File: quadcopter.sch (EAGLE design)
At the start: 65 parts, among them J1 AVR_SPI_PRG_6NS, U1 ATMEGA128RFA1, Y2 16MHz

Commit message: pinned up IMU
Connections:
- removed net VDD: C23.1, C24.1, U$8.VDD1, U$8.VDD2
- removed net VDDIO: C21.1, R12.2, R13.2, U$8.VDDIO1, U$8.VDDIO2
- net 3V: now also C21.1, C23.1, C24.1, R12.2, R13.2, U$8.CS_A/G, U$8.CS_M, U$8.DEN_A/G, U$8.DRDY_M, U$8.VDD1, U$8.VDD2, U$8.VDDIO1, U$8.VDDIO2
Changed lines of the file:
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@@
 <label x="193.04" y="30.48" size="1.778" layer="95" rot="R180" xref="yes"/>
+</segment>
+<segment>
+<pinref part="C21" gate="G$1" pin="1"/>
+<wire x1="180.34" y1="55.88" x2="180.34" y2="60.96" width="0.1524" layer="91"/>
+<label x="180.34" y="66.04" size="1.778" layer="95" rot="R90" xref="yes"/>
+<pinref part="U$8" gate="G$1" pin="VDDIO1"/>
+<wire x1="180.34" y1="60.96" x2="180.34" y2="66.04" width="0.1524" layer="91"/>
+<wire x1="220.98" y1="45.72" x2="220.98" y2="50.8" width="0.1524" layer="91"/>
+<pinref part="R12" gate="G$1" pin="2"/>
+<wire x1="220.98" y1="50.8" x2="220.98" y2="53.34" width="0.1524" layer="91"/>
+<wire x1="203.2" y1="50.8" x2="220.98" y2="50.8" width="0.1524" layer="91"/>
+<pinref part="R13" gate="G$1" pin="2"/>
+<wire x1="187.96" y1="50.8" x2="187.96" y2="53.34" width="0.1524" layer="91"/>
+<wire x1="187.96" y1="53.34" x2="220.98" y2="53.34" width="0.1524" layer="91"/>
+<wire x1="180.34" y1="60.96" x2="220.98" y2="60.96" width="0.1524" layer="91"/>
+<wire x1="220.98" y1="60.96" x2="220.98" y2="53.34" width="0.1524" layer="91"/>
+<junction x="180.34" y="60.96"/>
+<junction x="220.98" y="53.34"/>
+<junction x="220.98" y="50.8"/>
+</segment>
+<segment>
+<pinref part="U$8" gate="G$1" pin="VDDIO2"/>
+<wire x1="213.36" y1="35.56" x2="200.66" y2="35.56" width="0.1524" layer="91"/>
+<label x="200.66" y="35.56" size="1.778" layer="95" rot="R180" xref="yes"/>
+</segment>
+<segment>
+<pinref part="U$8" gate="G$1" pin="VDD1"/>
+<wire x1="226.06" y1="45.72" x2="226.06" y2="60.96" width="0.1524" layer="91"/>
+<pinref part="U$8" gate="G$1" pin="VDD2"/>
+<wire x1="228.6" y1="45.72" x2="228.6" y2="60.96" width="0.1524" layer="91"/>
+<wire x1="226.06" y1="60.96" x2="228.6" y2="60.96" width="0.1524" layer="91"/>
+<wire x1="228.6" y1="60.96" x2="228.6" y2="101.6" width="0.1524" layer="91"/>
+<pinref part="C24" gate="G$1" pin="1"/>
+<pinref part="C23" gate="G$1" pin="1"/>
+<wire x1="213.36" y1="96.52" x2="213.36" y2="99.06" width="0.1524" layer="91"/>
+<wire x1="213.36" y1="99.06" x2="205.74" y2="99.06" width="0.1524" layer="91"/>
+<wire x1="205.74" y1="99.06" x2="205.74" y2="96.52" width="0.1524" layer="91"/>
+<wire x1="228.6" y1="101.6" x2="213.36" y2="101.6" width="0.1524" layer="91"/>
+<wire x1="213.36" y1="101.6" x2="213.36" y2="99.06" width="0.1524" layer="91"/>
+<wire x1="213.36" y1="101.6" x2="213.36" y2="106.68" width="0.1524" layer="91"/>
+<junction x="213.36" y="99.06"/>
+<junction x="213.36" y="101.6"/>
+<junction x="228.6" y="60.96"/>
+<label x="213.36" y="106.68" size="1.778" layer="95" rot="R90" xref="yes"/>
+</segment>
+<segment>
+<pinref part="U$8" gate="G$1" pin="CS_A/G"/>
+<wire x1="223.52" y1="22.86" x2="223.52" y2="12.7" width="0.1524" layer="91"/>
+<wire x1="223.52" y1="12.7" x2="226.06" y2="12.7" width="0.1524" layer="91"/>
+<wire x1="226.06" y1="12.7" x2="228.6" y2="12.7" width="0.1524" layer="91"/>
+<wire x1="228.6" y1="12.7" x2="238.76" y2="12.7" width="0.1524" layer="91"/>
+<wire x1="238.76" y1="12.7" x2="241.3" y2="12.7" width="0.1524" layer="91"/>
+<wire x1="241.3" y1="12.7" x2="241.3" y2="10.16" width="0.1524" layer="91"/>
+<pinref part="U$8" gate="G$1" pin="CS_M"/>
+<wire x1="226.06" y1="22.86" x2="226.06" y2="12.7" width="0.1524" layer="91"/>
+<pinref part="U$8" gate="G$1" pin="DRDY_M"/>
+<wire x1="228.6" y1="22.86" x2="228.6" y2="12.7" width="0.1524" layer="91"/>
+<pinref part="U$8" gate="G$1" pin="DEN_A/G"/>
+<wire x1="238.76" y1="22.86" x2="238.76" y2="12.7" width="0.1524" layer="91"/>
+<junction x="226.06" y="12.7"/>
+<junction x="228.6" y="12.7"/>
+<junction x="238.76" y="12.7"/>
+<label x="241.3" y="10.16" size="1.778" layer="95" rot="R270" xref="yes"/>
 </segment>
 </net>
@@
 <wire x1="200.66" y1="38.1" x2="200.66" y2="40.64" width="0.1524" layer="91"/>
 <wire x1="200.66" y1="40.64" x2="198.12" y2="40.64" width="0.1524" layer="91"/>
+<junction x="203.2" y="38.1"/>
 </segment>
 </net>
@@
 <wire x1="187.96" y1="33.02" x2="185.42" y2="33.02" width="0.1524" layer="91"/>
 <label x="185.42" y="33.02" size="1.778" layer="95" rot="R180" xref="yes"/>
+<junction x="187.96" y="33.02"/>
 </segment>
 </net>
@@
 </segment>
 </net>
-<net name="VDDIO" class="0">
-<segment>
-<pinref part="U$8" gate="G$1" pin="VDDIO2"/>
-<wire x1="213.36" y1="35.56" x2="200.66" y2="35.56" width="0.1524" layer="91"/>
-<label x="200.66" y="35.56" size="1.778" layer="95" rot="R180" xref="yes"/>
-</segment>
-<segment>
-<pinref part="C21" gate="G$1" pin="1"/>
-<wire x1="180.34" y1="55.88" x2="180.34" y2="60.96" width="0.1524" layer="91"/>
-<label x="180.34" y="66.04" size="1.778" layer="95" rot="R90" xref="yes"/>
-<pinref part="U$8" gate="G$1" pin="VDDIO1"/>
-<wire x1="180.34" y1="60.96" x2="180.34" y2="66.04" width="0.1524" layer="91"/>
-<wire x1="220.98" y1="45.72" x2="220.98" y2="50.8" width="0.1524" layer="91"/>
-<pinref part="R12" gate="G$1" pin="2"/>
-<wire x1="220.98" y1="50.8" x2="220.98" y2="53.34" width="0.1524" layer="91"/>
-<wire x1="203.2" y1="50.8" x2="220.98" y2="50.8" width="0.1524" layer="91"/>
-<pinref part="R13" gate="G$1" pin="2"/>
-<wire x1="187.96" y1="50.8" x2="187.96" y2="53.34" width="0.1524" layer="91"/>
-<wire x1="187.96" y1="53.34" x2="220.98" y2="53.34" width="0.1524" layer="91"/>
-<wire x1="180.34" y1="60.96" x2="220.98" y2="60.96" width="0.1524" layer="91"/>
-<wire x1="220.98" y1="60.96" x2="220.98" y2="53.34" width="0.1524" layer="91"/>
-<junction x="180.34" y="60.96"/>
-<junction x="220.98" y="53.34"/>
-<junction x="220.98" y="50.8"/>
-</segment>
-</net>
 <net name="N$20" class="0">
 <segment>
@@
 </segment>
 </net>
-<net name="VDD" class="0">
-<segment>
-<pinref part="U$8" gate="G$1" pin="VDD1"/>
-<wire x1="226.06" y1="45.72" x2="226.06" y2="60.96" width="0.1524" layer="91"/>
-<pinref part="U$8" gate="G$1" pin="VDD2"/>
-<wire x1="228.6" y1="45.72" x2="228.6" y2="60.96" width="0.1524" layer="91"/>
-<wire x1="226.06" y1="60.96" x2="228.6" y2="60.96" width="0.1524" layer="91"/>
-<wire x1="228.6" y1="60.96" x2="228.6" y2="101.6" width="0.1524" layer="91"/>
-<pinref part="C24" gate="G$1" pin="1"/>
-<pinref part="C23" gate="G$1" pin="1"/>
-<wire x1="213.36" y1="96.52" x2="213.36" y2="99.06" width="0.1524" layer="91"/>
-<wire x1="213.36" y1="99.06" x2="205.74" y2="99.06" width="0.1524" layer="91"/>
-<wire x1="205.74" y1="99.06" x2="205.74" y2="96.52" width="0.1524" layer="91"/>
-<wire x1="228.6" y1="101.6" x2="213.36" y2="101.6" width="0.1524" layer="91"/>
-<wire x1="213.36" y1="101.6" x2="213.36" y2="99.06" width="0.1524" layer="91"/>
-<wire x1="213.36" y1="101.6" x2="213.36" y2="106.68" width="0.1524" layer="91"/>
-<junction x="213.36" y="99.06"/>
-<junction x="213.36" y="101.6"/>
-<junction x="228.6" y="60.96"/>
-<label x="213.36" y="106.68" size="1.778" layer="95" rot="R90" xref="yes"/>
-</segment>
-</net>

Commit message: pushing who am i and final changes to the IMU
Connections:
- net 3V: no longer U$8.DRDY_M
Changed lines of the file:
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@@
 <wire x1="223.52" y1="22.86" x2="223.52" y2="12.7" width="0.1524" layer="91"/>
 <wire x1="223.52" y1="12.7" x2="226.06" y2="12.7" width="0.1524" layer="91"/>
-<wire x1="226.06" y1="12.7" x2="228.6" y2="12.7" width="0.1524" layer="91"/>
-<wire x1="228.6" y1="12.7" x2="238.76" y2="12.7" width="0.1524" layer="91"/>
+<wire x1="226.06" y1="12.7" x2="238.76" y2="12.7" width="0.1524" layer="91"/>
 <wire x1="238.76" y1="12.7" x2="241.3" y2="12.7" width="0.1524" layer="91"/>
 <wire x1="241.3" y1="12.7" x2="241.3" y2="10.16" width="0.1524" layer="91"/>
 <pinref part="U$8" gate="G$1" pin="CS_M"/>
 <wire x1="226.06" y1="22.86" x2="226.06" y2="12.7" width="0.1524" layer="91"/>
-<pinref part="U$8" gate="G$1" pin="DRDY_M"/>
-<wire x1="228.6" y1="22.86" x2="228.6" y2="12.7" width="0.1524" layer="91"/>
 <pinref part="U$8" gate="G$1" pin="DEN_A/G"/>
 <wire x1="238.76" y1="22.86" x2="238.76" y2="12.7" width="0.1524" layer="91"/>
 <junction x="226.06" y="12.7"/>
-<junction x="228.6" y="12.7"/>
 <junction x="238.76" y="12.7"/>
 <label x="241.3" y="10.16" size="1.778" layer="95" rot="R270" xref="yes"/>

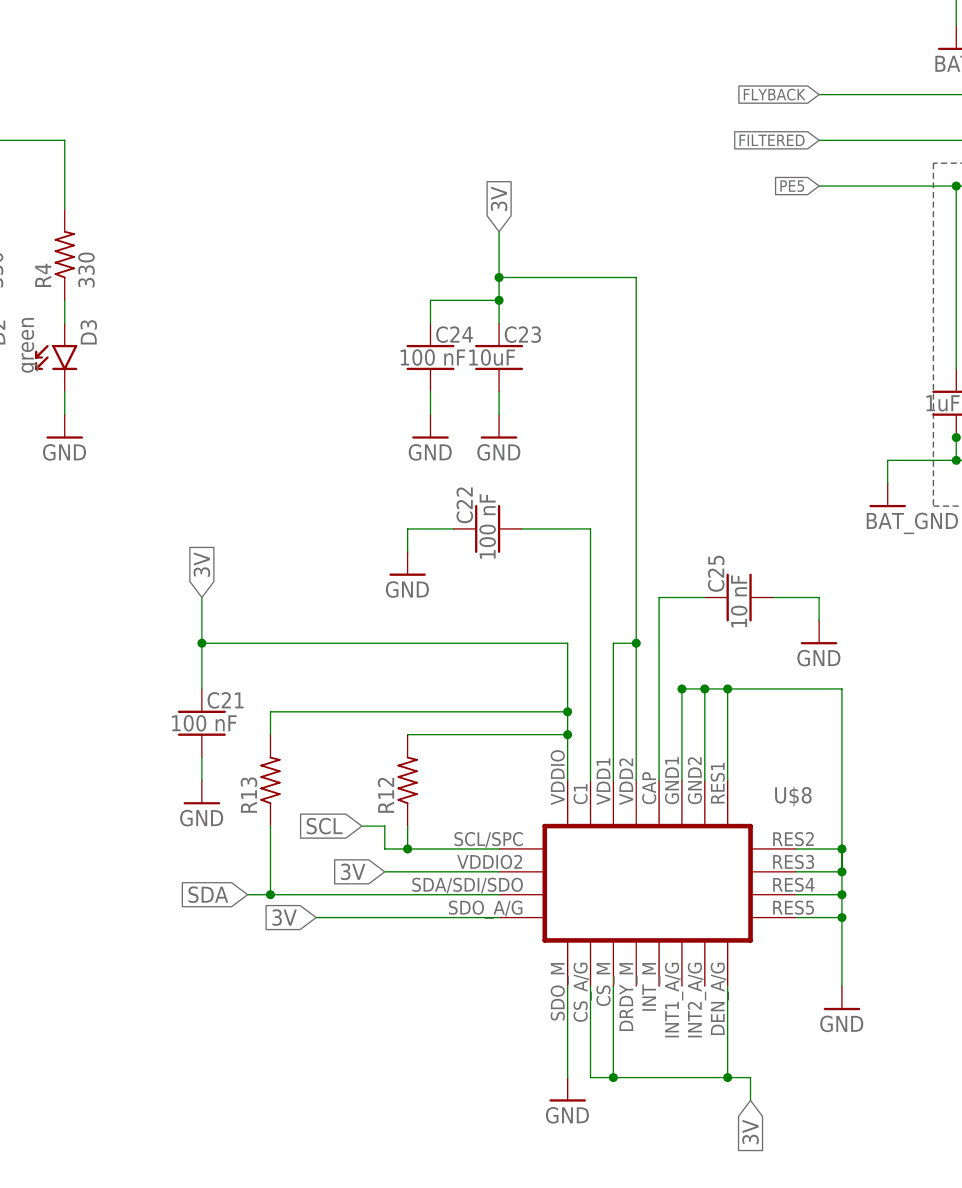
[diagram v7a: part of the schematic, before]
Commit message: Small fixes for IMU, added PID to who_am_i
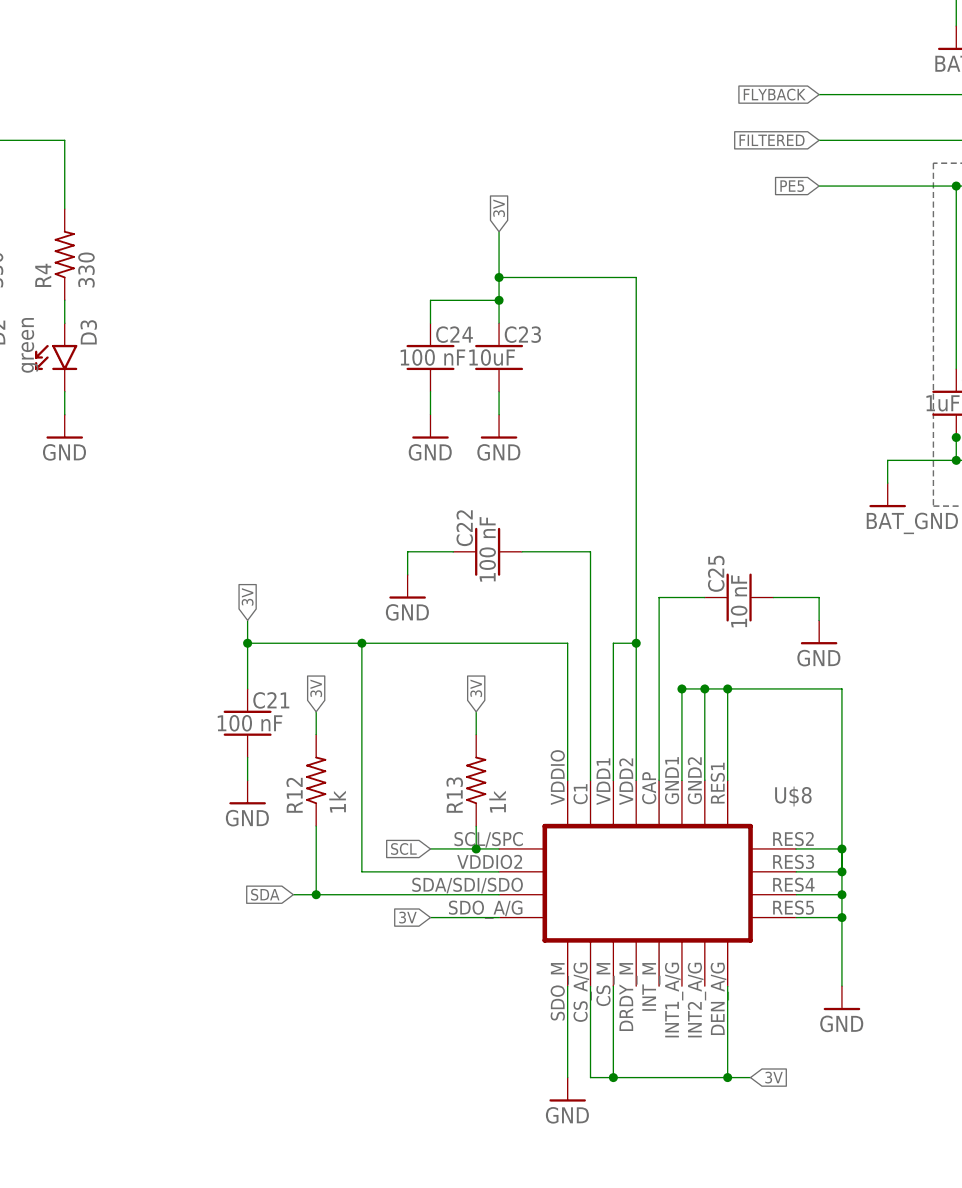
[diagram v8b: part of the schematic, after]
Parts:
- R12, R13: value (none) -> 1k
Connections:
- net SCL: now also R13.1; no longer R12.1
- net SDA: now also R12.1; no longer R13.1
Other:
- moved on the sheet: C21, C22, R12, R13
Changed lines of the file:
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@@
 <part name="U$7" library="quadparts" deviceset="MOSFET_20V" device=""/>
 <part name="U$8" library="quadparts" deviceset="IMU_9AXIS" device=""/>
-<part name="R12" library="quadparts_prebuilt" deviceset="RESISTOR_" device="SMD-2012-0805"/>
-<part name="R13" library="quadparts_prebuilt" deviceset="RESISTOR_" device="SMD-2012-0805"/>
 <part name="GND33" library="quadparts_prebuilt" deviceset="GND" device=""/>
 <part name="C21" library="quadparts_prebuilt" deviceset="CAPACITOR-NP_" device="SMD-2012-0805_CERAMIC" value="100 nF"/>
@@
 <part name="GND38" library="quadparts_prebuilt" deviceset="GND" device=""/>
 <part name="GND39" library="quadparts_prebuilt" deviceset="GND" device=""/>
+<part name="R12" library="quadparts_prebuilt" deviceset="RESISTOR_" device="SMD-2012-0805" value="1k"/>
+<part name="R13" library="quadparts_prebuilt" deviceset="RESISTOR_" device="SMD-2012-0805" value="1k"/>
 </parts>
 <sheets>
@@
 <instance part="U$7" gate="G$1" x="396.24" y="101.6"/>
 <instance part="U$8" gate="G$1" x="220.98" y="45.72"/>
-<instance part="R12" gate="G$1" x="203.2" y="45.72" rot="R90"/>
-<instance part="R13" gate="G$1" x="187.96" y="45.72" rot="R90"/>
 <instance part="GND33" gate="1" x="251.46" y="20.32"/>
-<instance part="C21" gate="G$1" x="180.34" y="53.34"/>
-<instance part="GND34" gate="1" x="180.34" y="43.18"/>
-<instance part="C22" gate="G$1" x="210.82" y="73.66" rot="R90"/>
-<instance part="GND35" gate="1" x="203.2" y="68.58"/>
+<instance part="C21" gate="G$1" x="185.42" y="53.34"/>
+<instance part="GND34" gate="1" x="185.42" y="43.18"/>
+<instance part="C22" gate="G$1" x="210.82" y="71.12" rot="R90"/>
+<instance part="GND35" gate="1" x="203.2" y="66.04"/>
 <instance part="GND36" gate="1" x="205.74" y="83.82"/>
 <instance part="GND37" gate="1" x="213.36" y="83.82"/>
@@
 <instance part="GND38" gate="1" x="248.92" y="60.96"/>
 <instance part="GND39" gate="1" x="220.98" y="10.16"/>
+<instance part="R12" gate="G$1" x="193.04" y="45.72" rot="R90"/>
+<instance part="R13" gate="G$1" x="210.82" y="45.72" rot="R90"/>
 </instances>
 <busses>
@@
 <segment>
 <pinref part="U$8" gate="G$1" pin="SDO_A/G"/>
-<wire x1="193.04" y1="30.48" x2="213.36" y2="30.48" width="0.1524" layer="91"/>
-<label x="193.04" y="30.48" size="1.778" layer="95" rot="R180" xref="yes"/>
+<wire x1="205.74" y1="30.48" x2="213.36" y2="30.48" width="0.1524" layer="91"/>
+<label x="205.74" y="30.48" size="1.27" layer="95" rot="R180" xref="yes"/>
 </segment>
 <segment>
 <pinref part="C21" gate="G$1" pin="1"/>
-<wire x1="180.34" y1="55.88" x2="180.34" y2="60.96" width="0.1524" layer="91"/>
-<label x="180.34" y="66.04" size="1.778" layer="95" rot="R90" xref="yes"/>
+<wire x1="185.42" y1="55.88" x2="185.42" y2="60.96" width="0.1524" layer="91"/>
+<label x="185.42" y="63.5" size="1.27" layer="95" rot="R90" xref="yes"/>
 <pinref part="U$8" gate="G$1" pin="VDDIO1"/>
-<wire x1="180.34" y1="60.96" x2="180.34" y2="66.04" width="0.1524" layer="91"/>
-<wire x1="220.98" y1="45.72" x2="220.98" y2="50.8" width="0.1524" layer="91"/>
-<pinref part="R12" gate="G$1" pin="2"/>
-<wire x1="220.98" y1="50.8" x2="220.98" y2="53.34" width="0.1524" layer="91"/>
-<wire x1="203.2" y1="50.8" x2="220.98" y2="50.8" width="0.1524" layer="91"/>
-<pinref part="R13" gate="G$1" pin="2"/>
-<wire x1="187.96" y1="50.8" x2="187.96" y2="53.34" width="0.1524" layer="91"/>
-<wire x1="187.96" y1="53.34" x2="220.98" y2="53.34" width="0.1524" layer="91"/>
-<wire x1="180.34" y1="60.96" x2="220.98" y2="60.96" width="0.1524" layer="91"/>
-<wire x1="220.98" y1="60.96" x2="220.98" y2="53.34" width="0.1524" layer="91"/>
-<junction x="180.34" y="60.96"/>
-<junction x="220.98" y="53.34"/>
-<junction x="220.98" y="50.8"/>
-</segment>
-<segment>
+<wire x1="185.42" y1="60.96" x2="185.42" y2="63.5" width="0.1524" layer="91"/>
+<wire x1="185.42" y1="60.96" x2="198.12" y2="60.96" width="0.1524" layer="91"/>
+<wire x1="198.12" y1="60.96" x2="220.98" y2="60.96" width="0.1524" layer="91"/>
+<wire x1="220.98" y1="60.96" x2="220.98" y2="45.72" width="0.1524" layer="91"/>
+<junction x="185.42" y="60.96"/>
 <pinref part="U$8" gate="G$1" pin="VDDIO2"/>
-<wire x1="213.36" y1="35.56" x2="200.66" y2="35.56" width="0.1524" layer="91"/>
-<label x="200.66" y="35.56" size="1.778" layer="95" rot="R180" xref="yes"/>
+<wire x1="213.36" y1="35.56" x2="198.12" y2="35.56" width="0.1524" layer="91"/>
+<wire x1="198.12" y1="35.56" x2="198.12" y2="60.96" width="0.1524" layer="91"/>
+<junction x="198.12" y="60.96"/>
 </segment>
 <segment>
@@
 <junction x="213.36" y="101.6"/>
 <junction x="228.6" y="60.96"/>
-<label x="213.36" y="106.68" size="1.778" layer="95" rot="R90" xref="yes"/>
+<label x="213.36" y="106.68" size="1.27" layer="95" rot="R90" xref="yes"/>
 </segment>
 <segment>
@@
 <wire x1="226.06" y1="12.7" x2="238.76" y2="12.7" width="0.1524" layer="91"/>
 <wire x1="238.76" y1="12.7" x2="241.3" y2="12.7" width="0.1524" layer="91"/>
-<wire x1="241.3" y1="12.7" x2="241.3" y2="10.16" width="0.1524" layer="91"/>
 <pinref part="U$8" gate="G$1" pin="CS_M"/>
 <wire x1="226.06" y1="22.86" x2="226.06" y2="12.7" width="0.1524" layer="91"/>
@@
 <junction x="226.06" y="12.7"/>
 <junction x="238.76" y="12.7"/>
-<label x="241.3" y="10.16" size="1.778" layer="95" rot="R270" xref="yes"/>
+<label x="241.3" y="12.7" size="1.27" layer="95" xref="yes"/>
+</segment>
+<segment>
+<wire x1="193.04" y1="50.8" x2="193.04" y2="53.34" width="0.1524" layer="91"/>
+<label x="193.04" y="53.34" size="1.27" layer="95" rot="R90" xref="yes"/>
+<pinref part="R12" gate="G$1" pin="2"/>
+</segment>
+<segment>
+<wire x1="210.82" y1="50.8" x2="210.82" y2="53.34" width="0.1524" layer="91"/>
+<label x="210.82" y="53.34" size="1.27" layer="95" rot="R90" xref="yes"/>
+<pinref part="R13" gate="G$1" pin="2"/>
 </segment>
 </net>
@@
 <pinref part="GND34" gate="1" pin="GND"/>
 <pinref part="C21" gate="G$1" pin="2"/>
-<wire x1="180.34" y1="45.72" x2="180.34" y2="48.26" width="0.1524" layer="91"/>
+<wire x1="185.42" y1="45.72" x2="185.42" y2="48.26" width="0.1524" layer="91"/>
 </segment>
 <segment>
@@
 <segment>
 <pinref part="GND35" gate="1" pin="GND"/>
-<wire x1="203.2" y1="71.12" x2="203.2" y2="73.66" width="0.1524" layer="91"/>
+<wire x1="203.2" y1="68.58" x2="203.2" y2="71.12" width="0.1524" layer="91"/>
 <pinref part="C22" gate="G$1" pin="1"/>
-<wire x1="203.2" y1="73.66" x2="208.28" y2="73.66" width="0.1524" layer="91"/>
+<wire x1="203.2" y1="71.12" x2="208.28" y2="71.12" width="0.1524" layer="91"/>
 </segment>
 <segment>
@@
 <segment>
 <pinref part="U$8" gate="G$1" pin="SCL/SPC"/>
-<wire x1="213.36" y1="38.1" x2="203.2" y2="38.1" width="0.1524" layer="91"/>
-<pinref part="R12" gate="G$1" pin="1"/>
-<wire x1="203.2" y1="38.1" x2="200.66" y2="38.1" width="0.1524" layer="91"/>
-<wire x1="203.2" y1="40.64" x2="203.2" y2="38.1" width="0.1524" layer="91"/>
-<label x="198.12" y="40.64" size="1.778" layer="95" rot="R180" xref="yes"/>
-<wire x1="200.66" y1="38.1" x2="200.66" y2="40.64" width="0.1524" layer="91"/>
-<wire x1="200.66" y1="40.64" x2="198.12" y2="40.64" width="0.1524" layer="91"/>
-<junction x="203.2" y="38.1"/>
+<wire x1="213.36" y1="38.1" x2="210.82" y2="38.1" width="0.1524" layer="91"/>
+<wire x1="210.82" y1="38.1" x2="205.74" y2="38.1" width="0.1524" layer="91"/>
+<wire x1="210.82" y1="40.64" x2="210.82" y2="38.1" width="0.1524" layer="91"/>
+<label x="205.74" y="38.1" size="1.27" layer="95" rot="R180" xref="yes"/>
+<junction x="210.82" y="38.1"/>
+<pinref part="R13" gate="G$1" pin="1"/>
 </segment>
 </net>
@@
 <segment>
 <pinref part="U$8" gate="G$1" pin="SDA/SDI/SDO"/>
-<wire x1="187.96" y1="33.02" x2="213.36" y2="33.02" width="0.1524" layer="91"/>
-<pinref part="R13" gate="G$1" pin="1"/>
-<wire x1="187.96" y1="40.64" x2="187.96" y2="33.02" width="0.1524" layer="91"/>
-<wire x1="187.96" y1="33.02" x2="185.42" y2="33.02" width="0.1524" layer="91"/>
-<label x="185.42" y="33.02" size="1.778" layer="95" rot="R180" xref="yes"/>
-<junction x="187.96" y="33.02"/>
+<wire x1="193.04" y1="33.02" x2="213.36" y2="33.02" width="0.1524" layer="91"/>
+<wire x1="193.04" y1="40.64" x2="193.04" y2="33.02" width="0.1524" layer="91"/>
+<wire x1="193.04" y1="33.02" x2="190.5" y2="33.02" width="0.1524" layer="91"/>
+<label x="190.5" y="33.02" size="1.27" layer="95" rot="R180" xref="yes"/>
+<junction x="193.04" y="33.02"/>
+<pinref part="R12" gate="G$1" pin="1"/>
 </segment>
 </net>
@@
 <pinref part="U$8" gate="G$1" pin="C1"/>
 <pinref part="C22" gate="G$1" pin="2"/>
-<wire x1="215.9" y1="73.66" x2="223.52" y2="73.66" width="0.1524" layer="91"/>
-<wire x1="223.52" y1="73.66" x2="223.52" y2="45.72" width="0.1524" layer="91"/>
-</segment>
-</net>
+<wire x1="215.9" y1="71.12" x2="223.52" y2="71.12" width="0.1524" layer="91"/>
+<wire x1="223.52" y1="71.12" x2="223.52" y2="45.72" width="0.1524" layer="91"/>
+</segment>
+</net>
